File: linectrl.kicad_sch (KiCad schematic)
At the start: 65 parts, among them J1 6P4C, J2 6P4C, J3 6P4C, J4 6P4C, K1 Relay_SPST-NO, K2 Relay_SPST-NO, K3 Relay_SPDT, K4 Relay_SPDT, Q1 PMOS, Q2 PMOS, Q3 PMOS, Q4 PMOS, T1 Transformer_1P_1S, T2 Transformer_1P_1S, U2 LM358

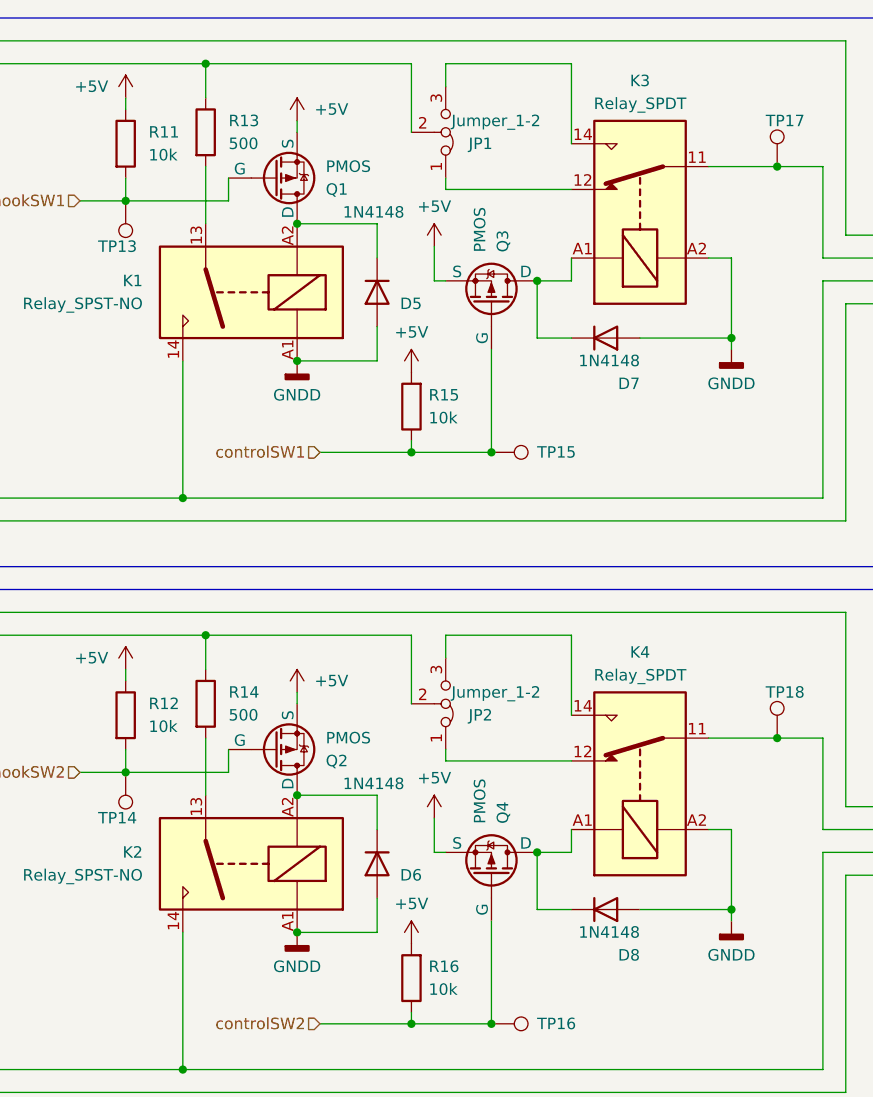
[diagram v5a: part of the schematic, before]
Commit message: continue pcb layout, finish linectrl layout
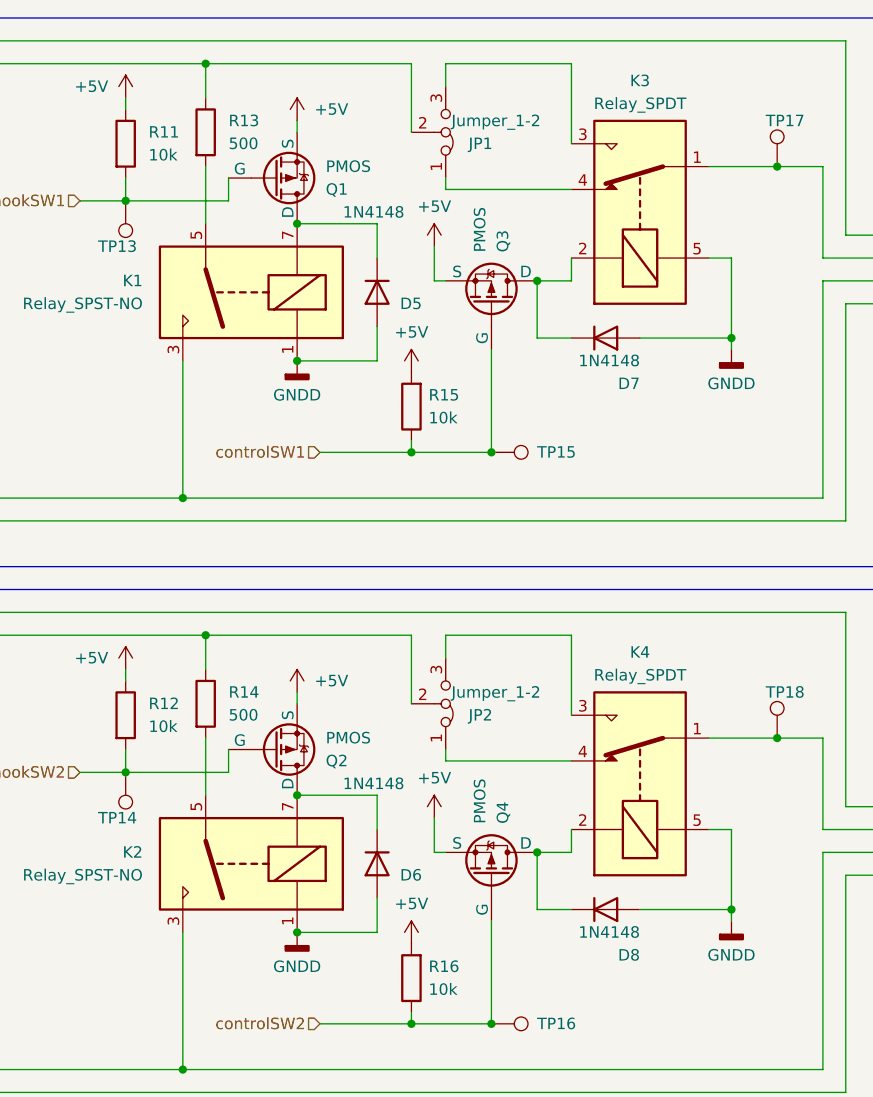
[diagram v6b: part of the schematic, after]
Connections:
- net GNDD: now also K1.1, K2.1, K3.5, K4.5; no longer K1.A1, K2.A1, K3.A2, K4.A2
- net at D8.1 (K), Q4.1 (D): now also K4.2; no longer K4.A1
- net at J4.3, TP18.1: now also K4.1; no longer K4.11
- net at R13.2: now also K1.5; no longer K1.13
- net at J1.3, J3.2, T1.2 (AB)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: now also K1.3; no longer K1.14
- net at D5.1 (K), Q1.1 (D): now also K1.7; no longer K1.A2
- net at J3.3, TP17.1: now also K3.1; no longer K3.11
- net at JP1.1 (A): now also K3.4; no longer K3.12
- net at JP1.3 (B): now also K3.3; no longer K3.14
- net at D7.1 (K), Q3.1 (D): now also K3.2; no longer K3.A1
- net at JP2.1 (A): now also K4.4; no longer K4.12
- net at JP2.3 (B): now also K4.3; no longer K4.14
- net at R14.2: now also K2.5; no longer K2.13
- net at J2.3, J4.2, T2.2 (AB)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: now also K2.3; no longer K2.14
- net at D6.1 (K), Q2.1 (D): now also K2.7; no longer K2.A2

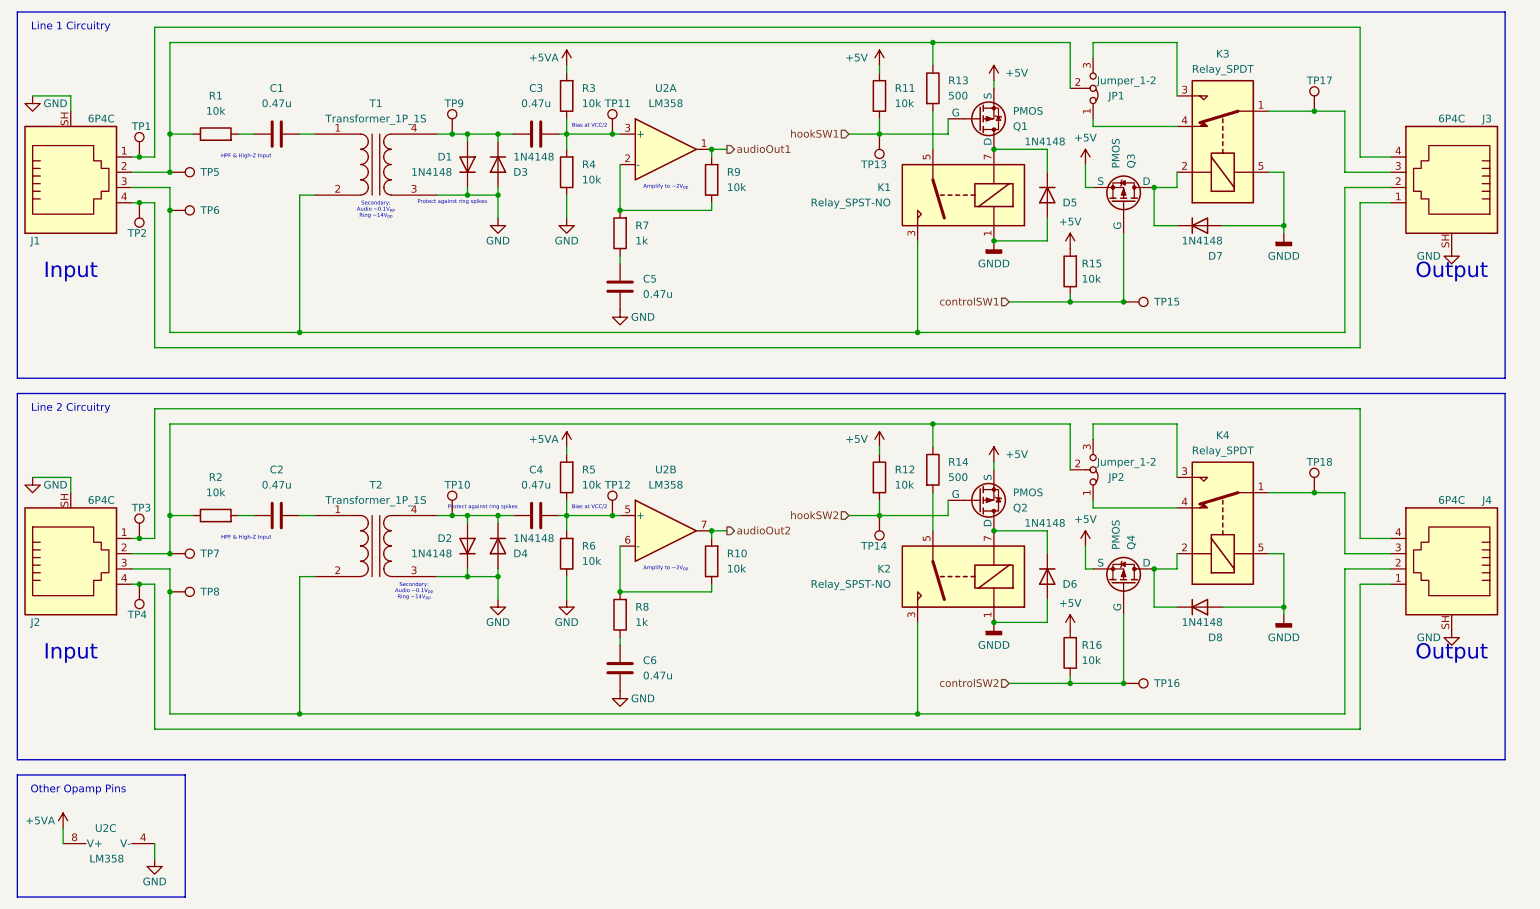
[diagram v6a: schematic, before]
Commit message: make each phone line a subsheet and start redoing layout
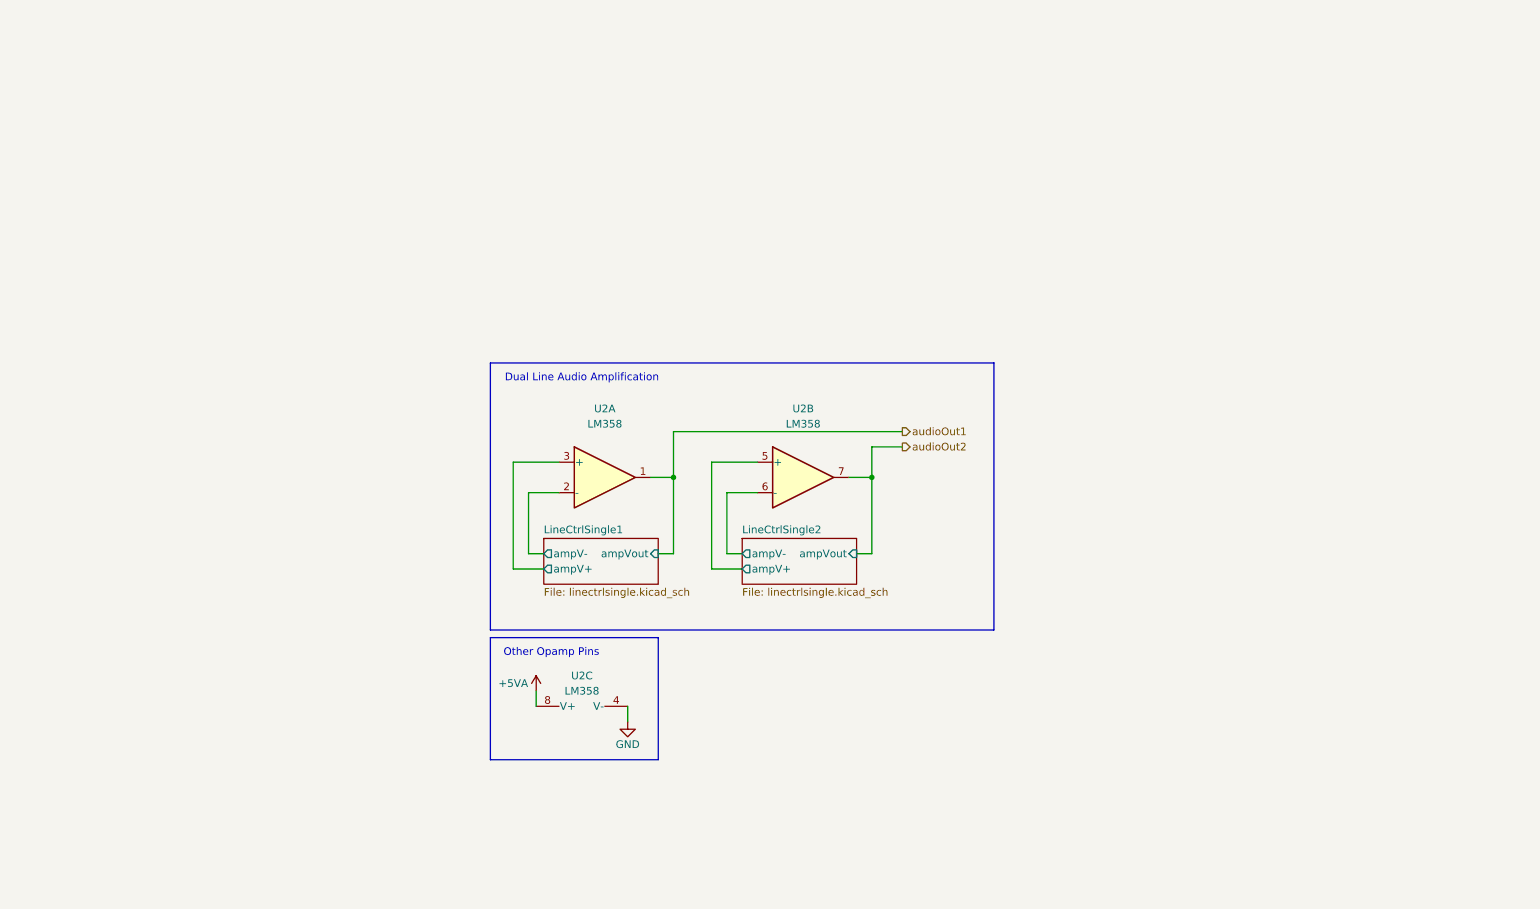
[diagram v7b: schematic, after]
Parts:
- removed C1, C2, C3, C4, C5, C6: 0.47u, Capacitor_THT:C_Rect_L7.0mm_W2.0mm_P5.00mm, symbol Device:C
- removed D1, D2, D3, D4, D5, D6, D7, D8: 1N4148, Diode_THT:D_DO-35_SOD27_P7.62mm_Horizontal, symbol Diode:1N4148
- removed J1, J2, J3, J4: 6P4C, Phones:CUI_CRJ050-1-TH, symbol Connector:6P4C_Shielded
- removed JP1, JP2: Jumper_1-2, Jumper:SolderJumper-3_P1.3mm_Bridged2Bar12_RoundedPad1.0x1.5mm, symbol Jumper:Jumper_3_Bridged12
- removed K1, K2: Relay_SPST-NO, Relay_THT:Relay_SPST_StandexMeder_SIL_Form1A, symbol Relay:Relay_SPST-NO
- removed K3, K4: Relay_SPDT, Phones:K_AZ943-1C_AMZ, symbol Relay:Relay_SPDT
- removed Q1, Q2, Q3, Q4: PMOS, Package_TO_SOT_THT:TO-92_HandSolder, symbol Simulation_SPICE:PMOS
- removed R1, R10, R2, R3, R4, R5, R6, R9: 10k, Resistor_THT:R_Axial_DIN0207_L6.3mm_D2.5mm_P7.62mm_Horizontal, symbol Device:R
- removed R11, R12, R15, R16: 10k, Resistor_THT:R_Axial_DIN0207_L6.3mm_D2.5mm_P10.16mm_Horizontal, symbol Device:R
- removed R13, R14: 500, Resistor_THT:R_Axial_DIN0207_L6.3mm_D2.5mm_P10.16mm_Horizontal, symbol Device:R
- removed R7, R8: 1k, Resistor_THT:R_Axial_DIN0207_L6.3mm_D2.5mm_P7.62mm_Horizontal, symbol Device:R
- removed T1, T2: Transformer_1P_1S, Phones:TY-145P, symbol Device:Transformer_1P_1S
- removed TP1, TP10, TP11, TP12, TP13, TP14, TP15, TP16, TP17, TP18, TP2, TP3, TP4, TP5, TP6, TP7, TP8, TP9: TestPoint, Testpoints:M5_3in1_TestPoint, symbol Connector:TestPoint
- U2: footprint Package_DIP:DIP-8_W7.62mm -> (none)
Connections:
- net LineCtrlSingle2/ampV+: now reaches U2.5 (+)
- net LineCtrlSingle2/ampV-: now reaches U2.6 (-)
- net LineCtrlSingle1/ampV-: now reaches U2.2 (-)
- net LineCtrlSingle1/ampV+: now reaches U2.3 (+)
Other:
- added sheet LineCtrlSingle1 (linectrlsingle.kicad_sch)
- added sheet LineCtrlSingle2 (linectrlsingle.kicad_sch)
- note added: "Dual Line Audio Amplification"
- note removed: "Amplify to ~2V_{pp}"
- note removed: "Bias at VCC/2"
- note removed: "HPF & High-Z Input"
- note removed: "Input"
- note removed: "Line 1 Circuitry"
- note removed: "Line 2 Circuitry"
- note removed: "Output"
- note removed: "Protect against ring spikes"
- note removed: "Secondary: Audio ~0.1V_{pp} Ring ~14V_{pp}"
